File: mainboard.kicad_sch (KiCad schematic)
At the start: 44 parts, among them J1 DRV8833-1, J10 Conn_02x04_Counter_Clockwise, J11 Conn_02x04_Counter_Clockwise, J12 Conn_02x04_Counter_Clockwise, J13 Conn_PCA9685, J2 DRV8833-0, J3 Conn_01x02, J4 Screw_Terminal_01x06, J5 Screw_Terminal_01x06, J6 VIM4_HEADER, J7 Conn_01x02, J8 Conn_01x02, J9 Conn_02x04_Counter_Clockwise, Q1 2N7000, Q2 2N7000, SW1 RotaryEncoder_Switch, SW3 SW_SPST, U1 MCP23017_SP, U2 PIC16F819-ISO

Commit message: Switches updated
Enumerated all switches in the VIM header and added their respective sub-circuitry. Fixed a few errors I was getting when I updated PCB from schematic.
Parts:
- added C10, C8, C9: 1uF, Capacitor_SMD:C_0805_2012Metric, symbol Device:C_Small
- added J14, J15, J16: Conn_01x02, Connector_PinHeader_2.54mm:PinHeader_1x02_P2.54mm_Vertical, symbol Connector_Generic:Conn_01x02
- added R11, R13, R15: 220, Resistor_SMD:R_0805_2012Metric, symbol Device:R_Small
- added R12, R14, R16: 10k, Resistor_SMD:R_0805_2012Metric, symbol Device:R_Small
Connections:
- net SWITCH is gone; now on net SW-L-A: C5.1, R6.2, R7.1
- net 3V_BUCK: now also J14.1 (Pin_1), J15.1 (Pin_1), J16.1 (Pin_1)
- net GND: now also C10.2, C8.2, C9.2, R12.2, R14.2, R16.2
- net SW-L-B: now also C8.1, R11.2, R12.1
- net SW-R-A: now also C9.1, R13.2, R14.1
- net SW-R-B: now also C10.1, R15.2, R16.1
- net CP-R-ENDSTOP1: now reaches RN1.13 (R12), U1.2 (GPB1)
- net CP-R-ENDSTOP0: now reaches RN1.14 (R13), U1.1 (GPB0)
- net CP-L-ENDSTOP1: now reaches RN1.2 (R1), U1.28 (GPA7)
- net CP-L-ENDSTOP0: now reaches RN1.3 (R2), U1.27 (GPA6)
- new net: J15.2 (Pin_2), R13.1
- new net: J14.2 (Pin_2), R11.1
- new net: J16.2 (Pin_2), R15.1
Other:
- note added: "DAUGHTERBOARD"
- note added: "SWITCH/BUTTON FILTER L-A"
- note added: "SWITCH/BUTTON FILTER L-B"
- note added: "SWITCH/BUTTON FILTER R-A"
- note added: "SWITCH/BUTTON FILTER R-B"
- note removed: "MOTOR SPEED CONTROL"
- note removed: "SWITCH/BUTTON FILTER"
- moved on the sheet: C3, C4, C6, C7, J6, J7, J8, Q1, Q2, R1, R10, R2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

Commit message: Fixed ERC complaints
Fixed the power and NC complaints issues when I tried to run the ERC check
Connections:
- net 3v3: no longer U1.9 (VDD)
- net PICO_3V3: now also U1.9 (VDD)
- net at RN1.10 (R9): no longer U1.5 (GPB4)
- net at RN1.11 (R10): no longer U1.4 (GPB3)
- net at RN1.12 (R11): no longer U1.3 (GPB2)
- now unconnected: U1.6 (GPB5), U1.7 (GPB6), U1.8 (GPB7)
- no-connect marks 31 -> 50
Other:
- moved on the sheet: Brd1

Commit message: The Great Simplification
Schematic:
Pico2 added, 12V buck added, Motor-Encoder Interface Added, PIC removed.

*No work yet on PCB, will chip away at orienting objects tomorrow.
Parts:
- removed C3, C4: 1uF, Capacitor_SMD:C_0805_2012Metric, symbol Device:C_Small
- removed C7: 0.1uF, Capacitor_SMD:C_0805_2012Metric, symbol Device:C_Small
- removed J7, J8: Conn_01x02, Connector_PinHeader_2.54mm:PinHeader_1x02_P2.54mm_Vertical, symbol Connector_Generic:Conn_01x02
- removed Q1, Q2: 2N7000, Package_TO_SOT_THT:TO-92_Inline, symbol Transistor_FET:2N7000
- removed R1, R8: 10k, Resistor_SMD:R_0805_2012Metric, symbol Device:R_Small
- removed R2, R3: 220, Resistor_SMD:R_0805_2012Metric, symbol Device:R_Small
- removed U2: PIC16F819-ISO, Package_SO:SOIC-18W_7.5x11.6mm_P1.27mm, symbol MCU_Microchip_PIC16:PIC16F819-ISO
- added A2: RaspberryPi_Pico, Module:RaspberryPi_Pico_Common_Unspecified, symbol MCU_Module:RaspberryPi_Pico
- added F5, F6: Fuse, Fuse:Fuseholder_Clip-5x20mm_Schurter_CQM_Inline_P20.60x5.00mm_D1.00mm_Horizontal, symbol Device:Fuse
- added J17, J26: Conn_02x04_Counter_Clockwise, Connector_PinHeader_2.54mm:PinHeader_2x04_P2.54mm_Vertical, symbol Connector_Generic:Conn_02x04_Counter_Clockwise
- added J18, J19, J20, J21, J22, J23, J7, J8: Screw_Terminal_01x06, Connector_PinHeader_2.54mm:PinHeader_1x06_P2.54mm_Vertical, symbol Connector:Screw_Terminal_01x06
- added J24: Screw_Terminal_01x04, Connector_PinHeader_2.54mm:PinHeader_1x04_P2.54mm_Vertical, symbol Connector:Screw_Terminal_01x04
- added J25: Screw_Terminal_01x02, Connector_PinHeader_2.54mm:PinHeader_1x02_P2.54mm_Vertical, symbol Connector:Screw_Terminal_01x02
- added Q3, Q4: 2N7000, Package_TO_SOT_THT:TO-92_Inline, symbol Transistor_FET:2N7000
- D1, SW3: footprint (none) -> LED_SMD:LED_0805_2012Metric_Pad1.15x1.40mm_HandSolder
- J6: footprint Connector_PinHeader_2.54mm:PinHeader_2x20_P2.54mm_Vertical -> Connector_IDC:IDC-Header_2x20_P2.54mm_Latch_Vertical
- R14: value 10k -> 220
- R15: value 220 -> 10k
- SW1: footprint Rotary_Encoder:RotaryEncoder_Alps_EC12E-Switch_Vertical_H20mm_CircularMountingHoles -> Rotary_Encoder:RotaryEncoder_Alps_EC11E-Switch_Vertical_H20mm
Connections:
- net PICO_3V3 is gone; now on net PICO1_3V3: A1.36 (3V3), Brd1.2 (VCC), J13.5 (Pin_5), U1.9 (VDD)
- net 3V_BUCK: no longer J15.1 (Pin_1), J16.1 (Pin_1), R9.1
- net 5V_BUCK: now also A1.39 (VSYS), A2.39 (VSYS), J18.2 (Pin_2), J19.2 (Pin_2), J20.2 (Pin_2), J21.2 (Pin_2), J22.2 (Pin_2), J23.2 (Pin_2), J7.2 (Pin_2), J8.2 (Pin_2); no longer A1.40 (VBUS)
- net 9V_BUCK: now also J25.1 (Pin_1)
- net CP-L: now also RN1.7 (R6), U1.23 (GPA2); no longer RN1.8 (R7), U1.22 (GPA1)
- net CP-R: now also RN1.6 (R5), U1.24 (GPA3); no longer RN1.7 (R6), U1.23 (GPA2)
- net DOOR-L: now also RN1.5 (R4), U1.25 (GPA4); no longer RN1.6 (R5), U1.24 (GPA3)
- net DOOR-R: now also RN1.4 (R3), U1.26 (GPA5); no longer RN1.5 (R4), U1.25 (GPA4)
- net GND: now also C10.1, C9.1, R15.2, A2.13 (GND), A2.18 (GND), A2.23 (GND), A2.28 (GND), A2.3 (GND), A2.38 (GND), A2.8 (GND), J17.3 (Pin_3), J17.4 (Pin_4), J17.5 (Pin_5), J17.6 (Pin_6), J18.1 (Pin_1), J19.1 (Pin_1), J20.1 (Pin_1), J21.1 (Pin_1), J22.1 (Pin_1), J23.1 (Pin_1), J24.2 (Pin_2), J24.3 (Pin_3), J25.2 (Pin_2), J26.3 (Pin_3), J26.4 (Pin_4), J26.5 (Pin_5), J26.6 (Pin_6), J7.1 (Pin_1), J8.1 (Pin_1), Q3.1 (S), Q4.1 (S); no longer C10.2, C6.2, C9.2, R14.2
- net GREEN: now also R15.1, Q3.2 (G)
- net LDR_ADC: now also A2.31 (GPIO26_ADC0)
- net MAIN_BUS: now also F5.1, F6.1
- net PIC_STATE: now also A2.21 (GPIO16)
- net RED: now also R16.1, Q4.2 (G)
- net START: now also C5.1, R6.2, R7.1
- net STOP: now also C8.1, R11.2, R12.1
- net TOTEM-EXTEND: now also RN1.12 (R11), U1.3 (GPB2); no longer RN1.4 (R3), U1.26 (GPA5)
- net COLL(en/dis): now reaches J6.38 (Pin_38)
- net SORT(en/dis): now reaches J6.39 (Pin_39)
- net at J15.2 (Pin_2): now also Q3.3 (D); no longer R13.1
- net at J16.2 (Pin_2): now also Q4.3 (D); no longer R15.1
- net 12V_BUCK renamed 12V_BUCK1
- net 12V_BUCK1: now also J24.1 (Pin_1); no longer J1.3 (Pin_3), J2.3 (Pin_3)
- net 3v3 renamed PICO1_3V3
- net AGND renamed AGND1
- net COLL/SORT(en/dis) renamed COLL/(en/dis)
- net COLL/(en/dis): no longer J6.22 (Pin_22)
- net HEADLIGHTS: no longer names the net of J6.30 (Pin_30)
- removed net SW-L-A: C5.1, J6.33 (Pin_33), R6.2, R7.1
- removed net SW-L-B: C8.1, J6.35 (Pin_35), R11.2, R12.1
- removed net SW-R-A: C9.1, J6.36 (Pin_36), R13.2, R14.1
- removed net SW-R-B: C10.1, J6.37 (Pin_37), R15.2, R16.1
- new net: C10.2, J16.1 (Pin_1), R14.2
- new net: C9.2, J15.1 (Pin_1), R13.2
- new net: J22.3 (Pin_3), J23.3 (Pin_3)
- new net: J22.4 (Pin_4), J23.4 (Pin_4)
- new net: J22.5 (Pin_5), J23.5 (Pin_5)
- new net: J22.6 (Pin_6), J23.6 (Pin_6)
- new net: F6.2, J26.1 (Pin_1), J26.2 (Pin_2)
- new net: J7.3 (Pin_3), J8.3 (Pin_3)
- new net: J7.4 (Pin_4), J8.4 (Pin_4)
- new net: J7.5 (Pin_5), J8.5 (Pin_5)
- new net: J7.6 (Pin_6), J8.6 (Pin_6)
- new net: J20.3 (Pin_3), J21.3 (Pin_3)
- new net: J20.4 (Pin_4), J21.4 (Pin_4)
- new net: J20.5 (Pin_5), J21.5 (Pin_5)
- new net: J20.6 (Pin_6), J21.6 (Pin_6)
- new net: J18.3 (Pin_3), J19.3 (Pin_3)
- new net: J18.4 (Pin_4), J19.4 (Pin_4)
- new net: J18.5 (Pin_5), J19.5 (Pin_5)
- new net: J18.6 (Pin_6), J19.6 (Pin_6)
- new net: F5.2, J17.1 (Pin_1), J17.2 (Pin_2)
- new net 12V_BUCK2: J17.7 (Pin_7), J17.8 (Pin_8), J24.4 (Pin_4), R13.1, R14.1
- new net 12V_BUCK3: J1.3 (Pin_3), J2.3 (Pin_3), J26.7 (Pin_7), J26.8 (Pin_8)
- new net AGND2: A2.33 (AGND), C6.2
- new net BOOM(ext/ret): J6.33 (Pin_33)
- new net PICO2_3V3: A2.36 (3V3), R9.1
- new net SORT/(en/dis): RN1.8 (R7), U1.22 (GPA1)
- no-connect marks 50 -> 66
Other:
- note added: "DAUGHTERBOARD A"
- note added: "DAUGHTERBOARD B"
- note added: "GREEN"
- note added: "MOTOR-ENCODER INTERFACE"
- note added: "Motor Controller Power"
- note added: "Motor Interface"
- note added: "RED"
- note added: "SWITCH/BUTTON START"
- note added: "SWITCH/BUTTON STOP"
- note added: "VIM4 MOLEX"
- note removed: "DAUGHTERBOARD"
- note removed: "PIC FOR ADC SIG"
- note removed: "SWITCH/BUTTON FILTER L-A"
- note removed: "SWITCH/BUTTON FILTER L-B"
- note removed: "SWITCH/BUTTON FILTER R-A"
- note removed: "SWITCH/BUTTON FILTER R-B"
- note removed: "VOLTAGE CONTROLLER FOR LEDS"
- moved on the sheet: C5, C6, C8, D1, F1, F2, J11, J12, J14, J3, J6, R10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

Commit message: First full buildup for the PCB
Board1, bucks removed. Motor interface added,
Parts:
- removed C1, C2: 1uF, Capacitor_SMD:C_0805_2012Metric, symbol Device:C_Small
- removed D1: LED_Small, LED_SMD:LED_0805_2012Metric_Pad1.15x1.40mm_HandSolder, symbol Device:LED_Small
- removed F1, F2, F3, F4, F5, F6: Fuse, Fuse:Fuseholder_Clip-5x20mm_Schurter_CQM_Inline_P20.60x5.00mm_D1.00mm_Horizontal, symbol Device:Fuse
- removed J10, J11, J12, J17, J26, J9: Conn_02x04_Counter_Clockwise, Connector_PinHeader_2.54mm:PinHeader_2x04_P2.54mm_Vertical, symbol Connector_Generic:Conn_02x04_Counter_Clockwise
- removed R9: LDR07, OptoDevice:R_LDR_5.1x4.3mm_P3.4mm_Vertical, symbol Sensor_Optical:LDR07
- removed SW1: RotaryEncoder_Switch, Rotary_Encoder:RotaryEncoder_Alps_EC11E-Switch_Vertical_H20mm, symbol Device:RotaryEncoder_Switch
- removed SW3: SW_SPST, LED_SMD:LED_0805_2012Metric_Pad1.15x1.40mm_HandSolder, symbol Switch:SW_SPST
- added C11, C7: 1uF, Capacitor_SMD:C_0805_2012Metric, symbol Device:C_Small
- added J27: Rotary Encoder Conn, Connector_JST:JST_EH_B4B-EH-A_1x04_P2.50mm_Vertical, symbol Connector_Generic:Conn_01x04
- added J28: Conn_01x02, Connector_JST:JST_EH_B2B-EH-A_1x02_P2.50mm_Vertical, symbol Connector_Generic:Conn_01x02
- J18, J19, J20, J21, J22, J23, J7, J8: footprint Connector_PinHeader_2.54mm:PinHeader_1x06_P2.54mm_Vertical -> TerminalBlock:TerminalBlock_Xinya_XY308-2.54-6P_1x06_P2.54mm_Horizontal
- J6: footprint Connector_IDC:IDC-Header_2x20_P2.54mm_Latch_Vertical -> Connector_IDC:IDC-Header_2x20_P2.54mm_Vertical
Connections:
- net COLL/(en/dis) is gone; now on net COLL(en/dis): RN1.9 (R8), U1.21 (GPA0)
- net SORT/(en/dis) is gone; now on net SORT(en/dis): RN1.8 (R7), U1.22 (GPA1)
- net AGND1: now also C11.2, C7.2, J27.4 (Pin_4)
- net LDR_ADC: now also J28.2 (Pin_2)
- net PICO2_3V3: now also J28.1 (Pin_1)
- net PIC_STATE: now also J6.31 (Pin_31); no longer J6.32 (Pin_32)
- net TOTEM-EXTEND: now also J6.32 (Pin_32); no longer J6.31 (Pin_31)
- net ADC0_GP26: now reaches A1.31 (GPIO26_ADC0)
- net ADC0_GP26: now also C11.1, J27.1 (Pin_1)
- net ADC1_GP27: now reaches A1.32 (GPIO27_ADC1)
- net ADC1_GP27: now also C7.1, J27.2 (Pin_2)
- net ADC2_GP28: now reaches A1.34 (GPIO28_ADC2)
- net ADC2_GP28: now also J27.3 (Pin_3)
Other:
- note removed: "12V BUCK"
- note removed: "3V BUCK"
- note removed: "5V BUCK"
- note removed: "9V BUCK"
- note removed: "MAIN ON/OFF - EMERGENCY SWITCH"

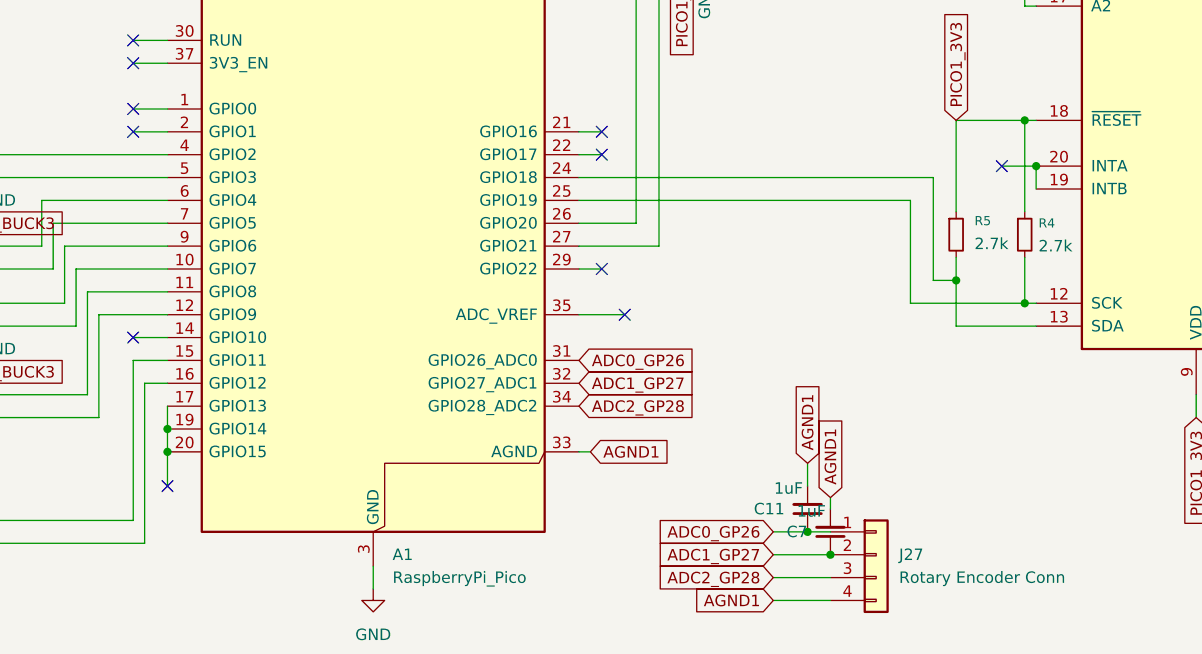
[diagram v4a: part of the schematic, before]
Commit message: 0 Error DRC mainboard V1
completed digital rules check and electrical rules check. ready to export to gerber
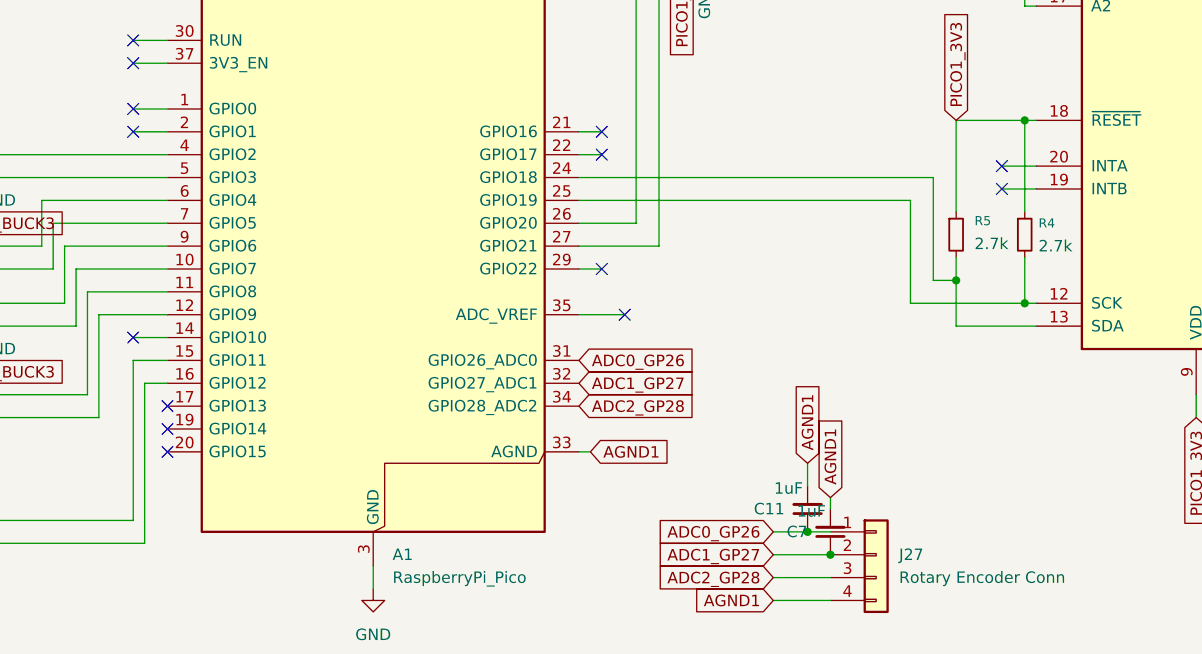
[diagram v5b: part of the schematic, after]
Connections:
- net at U1.19 (INTB): no longer U1.20 (INTA)
- now unconnected: A1.17 (GPIO13), A1.19 (GPIO14), A1.20 (GPIO15)
- no-connect marks 66 -> 69
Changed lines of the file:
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@@
-	)
-	(junction
-		(at 85.09 93.98)
-		(diameter 0)
-		(color 0 0 0 0)
 	)
 	(junction
@@
 	)
 	(junction
-		(at 181.61 64.77)
-		(diameter 0)
-		(color 0 0 0 0)
-	)
-	(junction
 		(at 101.6 322.58)
 		(diameter 0)
@@
 	)
 	(junction
-		(at 85.09 96.52)
-		(diameter 0)
-		(color 0 0 0 0)
-	)
-	(junction
 		(at 118.11 374.65)
 		(diameter 0)
@@
 	)
 	(no_connect
-		(at 85.09 100.33)
-	)
-	(no_connect
 		(at 22.86 176.53)
 	)
 	(no_connect
+		(at 85.09 96.52)
+	)
+	(no_connect
 		(at 22.86 199.39)
 	)
@@
 	)
 	(no_connect
+		(at 177.8 67.31)
+	)
+	(no_connect
 		(at 220.98 69.85)
 	)
@@
 	)
 	(no_connect
+		(at 85.09 91.44)
+	)
+	(no_connect
 		(at 288.29 143.51)
 	)
@@
 	)
 	(no_connect
+		(at 85.09 93.98)
+	)
+	(no_connect
 		(at 81.28 83.82)
 	)
@@
 	(wire
 		(pts
-			(xy 85.09 93.98) (xy 85.09 96.52)
-		)
-		(stroke
-			(width 0)
-			(type default)
-		)
-	)
-	(wire
-		(pts
 			(xy 130.81 63.5) (xy 133.35 63.5)
 		)
@@
 	(wire
 		(pts
-			(xy 85.09 91.44) (xy 85.09 93.98)
-		)
-		(stroke
-			(width 0)
-			(type default)
-		)
-	)
-	(wire
-		(pts
 			(xy 288.29 156.21) (xy 293.37 156.21)
 		)
@@
 	(wire
 		(pts
-			(xy 181.61 64.77) (xy 181.61 67.31)
-		)
-		(stroke
-			(width 0)
-			(type default)
-		)
-	)
-	(wire
-		(pts
 			(xy 137.16 299.72) (xy 142.24 299.72)
 		)
@@
 	(wire
 		(pts
-			(xy 85.09 96.52) (xy 85.09 100.33)
-		)
-		(stroke
-			(width 0)
-			(type default)
-		)
-	)
-	(wire
-		(pts
 			(xy 217.17 41.91) (xy 242.57 41.91)
 		)
@@
 		)
 		(stroke
+			(width 0)
+			(type default)
+		)
+	)
+	(wire
+		(pts
+			(xy 177.8 67.31) (xy 181.61 67.31)
+		)
+		(stroke

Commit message: Validated mainboard V1.15
0 Error 0 Warnings

Ready for Ochoa chack
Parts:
- RN1: footprint Resistor_THT:R_Array_SIP14 -> Package_DIP:DIP-14_W7.62mm
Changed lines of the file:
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@@
 			)
 		)
-		(property "Footprint" "Resistor_THT:R_Array_SIP14"
+		(property "Footprint" "Package_DIP:DIP-14_W7.62mm"
 			(at 254 76.835 90)
 			(effects
